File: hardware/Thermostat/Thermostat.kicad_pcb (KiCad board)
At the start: 2 copper layers, 111.2 x 76.5 mm, 46 parts, among them J1 Barrel_Jack_Switch, J2 Conn_01x02_Pin, J3 AVR-ISP-6, J4 MainConnectorr, K1 G6E, K2 G6E, K3 G6E, K4 G6E, SW1 12MM, SW2 12MM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

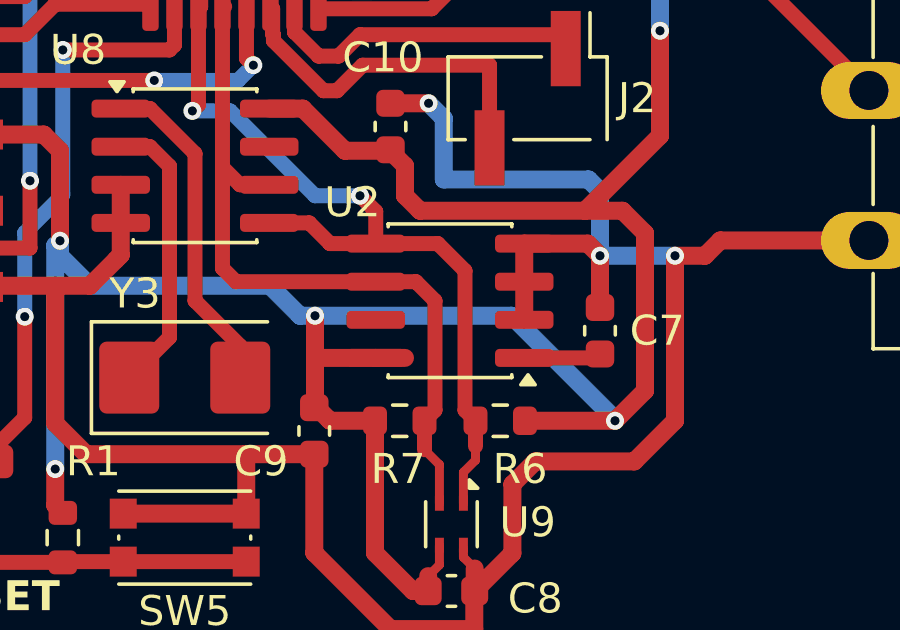
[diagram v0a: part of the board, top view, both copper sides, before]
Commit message: Integrate 47L04
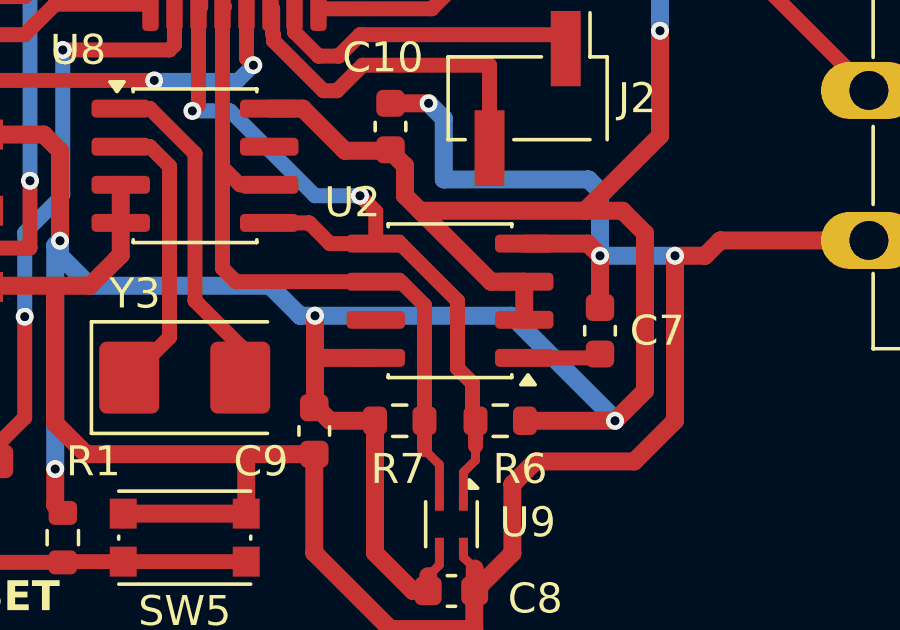
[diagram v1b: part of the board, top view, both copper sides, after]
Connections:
- U2 pad 2: GND -> +5V
- U2 pad 3: GND -> +5V
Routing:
- net +5V: track 189.7 -> 194.4 mm
- net GND: track 476.3 -> 473.8 mm
- net I2C_SDA: track 78.3 -> 77.6 mm
- net I2C_SCL: track 76.8 -> 76.3 mm
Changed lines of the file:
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@@
 			(layers "F.Cu" "F.Mask" "F.Paste")
 			(roundrect_rratio 0.25)
-			(net 1 "GND")
+			(net 3 "+5V")
 			(pinfunction "A1")
 			(pintype "input")
@@
 			(layers "F.Cu" "F.Mask" "F.Paste")
 			(roundrect_rratio 0.25)
-			(net 1 "GND")
+			(net 3 "+5V")
 			(pinfunction "A2")
 			(pintype "input")
@@
 	)
 	(segment
-		(start 195.975 110.595)
-		(end 195.975 113.135)
-		(width 0.6)
-		(layer "F.Cu")
-		(net 1)
-	)
-	(segment
 		(start 140.958 121.188)
 		(end 141.05 121.096)
@@
 	)
 	(segment
+		(start 195.975 111.865)
+		(end 195.975 113.135)
+		(width 0.6)
+		(layer "F.Cu")
+		(net 3)
+	)
+	(segment
 		(start 188.595 106.095)
 		(end 190 107.5)
@@
 	)
 	(segment
-		(start 191.999999 114.405)
-		(end 191.025 114.405)
+		(start 194.865 111.865)
+		(end 195.975 111.865)
+		(width 0.6)
+		(layer "F.Cu")
+		(net 3)
+	)
+	(segment
+		(start 192.5 109.5)
+		(end 194.865 111.865)
 		(width 0.6)
 		(layer "F.Cu")
@@
 	)
 	(segment
-		(start 194 111.5)
-		(end 194 116.15)
-		(width 0.5)
-		(layer "F.Cu")
-		(net 20)
-	)
-	(segment
 		(start 193.948 118.218)
 		(end 194.35 117.816)
@@
 	)
 	(segment
-		(start 194.35 117.348)
-		(end 194.35 116.5)
+		(start 193.75 112.5)
+		(end 193.75 114.75)
 		(width 0.5)
 		(layer "F.Cu")
@@
 	)
 	(segment
-		(start 188.214 58.418)
-		(end 185.003 55.207)
+		(start 194.35 117.348)
+		(end 194.35 116.5)
 		(width 0.5)
 		(layer "F.Cu")
@@
 	)
 	(segment
-		(start 191.025 110.595)
-		(end 193.095 110.595)
+		(start 188.214 58.418)
+		(end 185.003 55.207)
 		(width 0.5)
 		(layer "F.Cu")
@@
 	)
 	(segment
-		(start 193.095 110.595)
-		(end 194 111.5)
+		(start 191.845 110.595)
+		(end 193.75 112.5)
 		(width 0.5)
 		(layer "F.Cu")
@@
 	)
 	(segment
+		(start 194.25 115.25)
+		(end 194.25 116.4)
+		(width 0.5)
+		(layer "F.Cu")
+		(net 20)
+	)
+	(segment
 		(start 185.166 79.248)
 		(end 185.166 88.392)
@@
 	)
 	(segment
-		(start 189.5 110.595)
-		(end 191.025 110.595)
+		(start 193.75 114.75)
+		(end 194.25 115.25)
+		(width 0.5)
+		(layer "F.Cu")
+		(net 20)
+	)
+	(segment
+		(start 194.25 116.4)
+		(end 194.35 116.5)
+		(width 0.5)
+		(layer "F.Cu")
+		(net 20)
+	)
+	(segment
+		(start 191.025 110.595)
+		(end 191.845 110.595)
 		(width 0.5)
 		(layer "F.Cu")
@@
 	(segment
 		(start 189.5 110.595)
-		(end 188.81 109.905)
+		(end 191.025 110.595)
 		(width 0.5)
 		(layer "F.Cu")
@@
 	)
 	(segment
-		(start 194 116.15)
-		(end 194.35 116.5)
+		(start 189.5 110.595)
+		(end 188.81 109.905)
 		(width 0.5)
 		(layer "F.Cu")
@@
 	)
 	(segment
+		(start 191.025 111.865)
+		(end 191.865 111.865)
+		(width 0.5)
+		(layer "F.Cu")
+		(net 21)
+	)
+	(segment
 		(start 186.69 92.456)
 		(end 186.69 81.28)
@@
 	)
 	(segment
-		(start 192.65 117.466)
-		(end 193.148 117.964)
-		(width 0.3)
+		(start 191.865 111.865)
+		(end 192.65 112.65)
+		(width 0.5)
 		(layer "F.Cu")
 		(net 21)
 	)
 	(segment
-		(start 193 112.5)
-		(end 193 116.15)
-		(width 0.5)
+		(start 192.65 117.466)
+		(end 193.148 117.964)
+		(width 0.3)
 		(layer "F.Cu")
 		(net 21)
 	)
 	(segment
-		(start 192.365 111.865)
-		(end 193 112.5)
+		(start 192.65 112.65)
+		(end 192.65 116.5)
 		(width 0.5)
 		(layer "F.Cu")
@@
 		(width 0.5)
 		(layer "F.Cu")
-		(net 21)
-	)
-	(segment
-		(start 191.025 111.865)
-		(end 192.365 111.865)
-		(width 0.5)
-		(layer "F.Cu")
-		(net 21)
-	)
-	(segment
-		(start 193 116.15)
-		(end 192.65 116.5)
-		(width 0.5)
-		(layer "F.Cu")

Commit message: Battery?
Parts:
- added BT1: Battery_Cell, Battery:BatteryHolder_LINX_BAT-HLD-012-SMT, B.Cu at (172.0, 62.2)
- moved R1 0.34 mm to (180.2, 120.4)
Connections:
- U8 pad 3: GND -> Net-(BT1-+)
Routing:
- net GND: track 473.8 -> 472.5 mm

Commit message: Get in battery
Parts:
- BT1: footprint Battery:BatteryHolder_LINX_BAT-HLD-012-SMT -> Battery:BatteryHolder_Keystone_3000_1x12mm
- moved BT1 2.68 mm to (171.1, 64.8)
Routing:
- net Net-(BT1-+): track 0.00 -> 77.5 mm, vias 0 -> 1
- net GND: track 472.5 -> 481.1 mm, vias 11 -> 12
- net Net-(J3-SCK): track 25.4 -> 23.0 mm
- net +5V: track 194.0 -> 192.5 mm

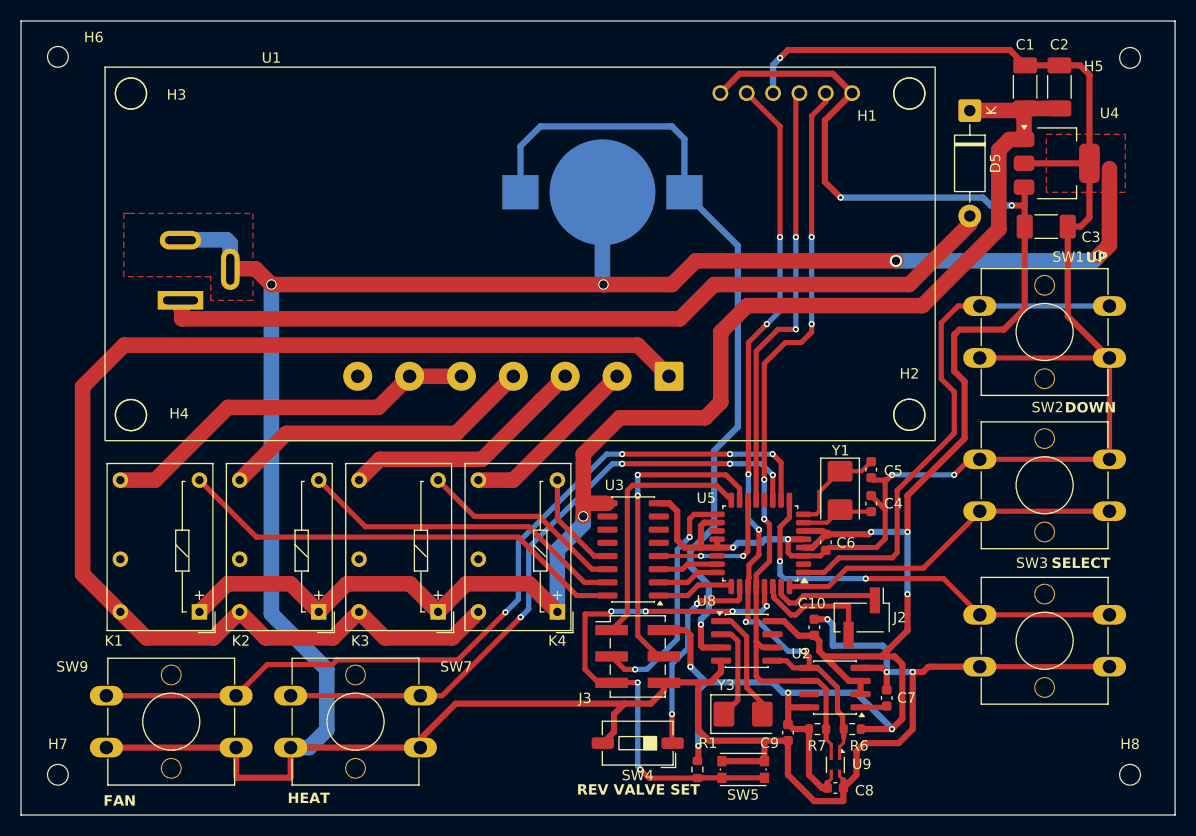
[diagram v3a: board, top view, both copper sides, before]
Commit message: Good battery and connector layout
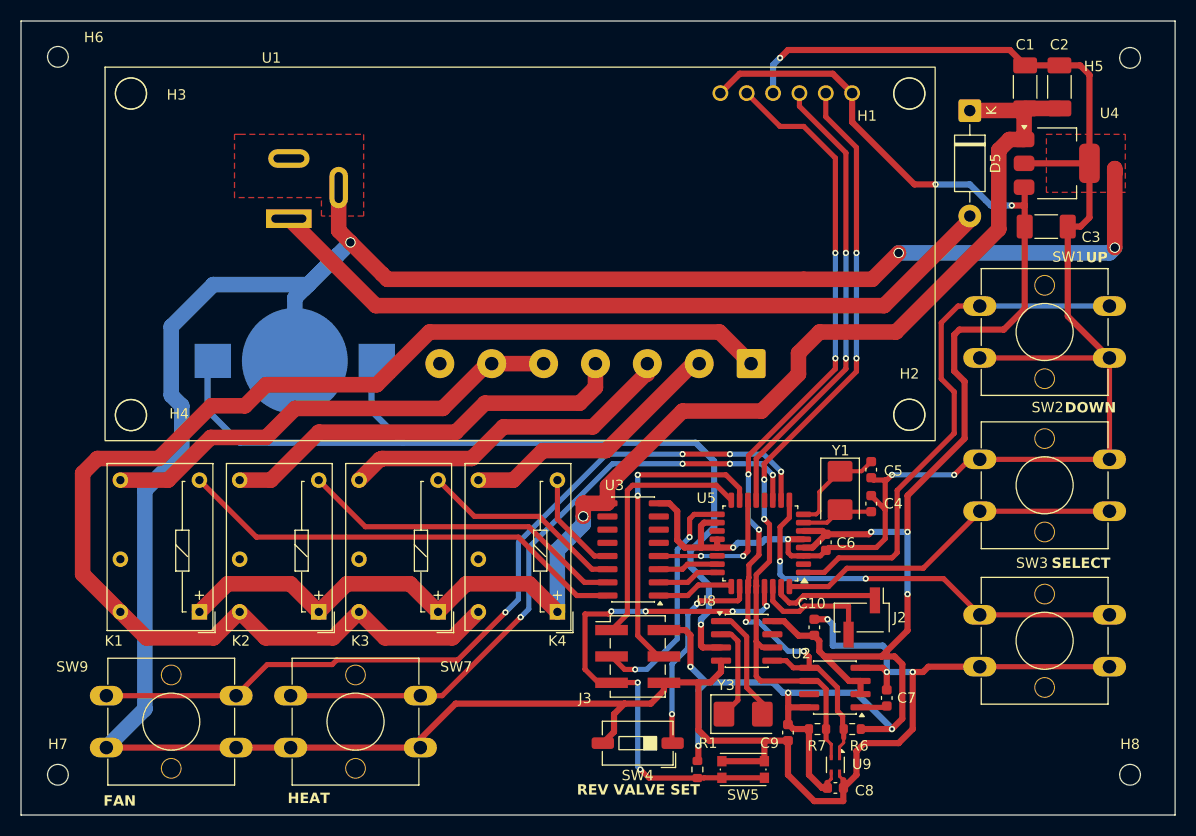
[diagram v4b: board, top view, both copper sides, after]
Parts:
- moved BT1 33.8 mm to (141.5, 81.0)
- moved J1 13.1 mm to (140.9, 67.3)
- moved J4 8.01 mm to (185.4, 81.3)
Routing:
- net Net-(J4-Pin_4): track 30.5 -> 40.3 mm
- net Net-(BT1-+): track 77.5 -> 86.6 mm
- net Net-(D5-A): track 81.6 -> 72.9 mm
- net Net-(J4-Pin_5): track 37.0 -> 45.4 mm
- net Net-(J4-Pin_2): track 17.5 -> 25.9 mm
- net Net-(J4-Pin_3): track 24.0 -> 32.0 mm
- net +5V: track 192.5 -> 185.4 mm
- net 24VDC: track 133.9 -> 127.2 mm
- net I2C_SDA: track 77.6 -> 83.3 mm
- net 24VAC: track 123.3 -> 126.9 mm
- net SCBUSY: track 42.0 -> 45.2 mm
- net GND: track 481.1 -> 482.9 mm, vias 12 -> 11
- net I2C_SCL: track 76.3 -> 77.8 mm
- net Net-(U5-PD6): track 81.9 -> 81.3 mm

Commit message: Always changes
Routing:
- net Net-(J4-Pin_4): track 40.3 -> 39.1 mm

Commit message: Fixes from Cyber City Circuits review
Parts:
- removed D5: 1N4007, Diode_THT:D_DO-41_SOD81_P10.16mm_Horizontal
- added D1: SS33, Diode_SMD:D_SMA, F.Cu at (206.0, 63.5)
- added R2: 4.7k, Resistor_SMD:R_0603_1608Metric, F.Cu at (197.4, 66.8)
- R1: value 5k -> 10k
- R6, R7: value 5k -> 4.7k
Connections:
- U1 pad 6: +5V -> ^SCRESET
- U5 pad 12: unconnected-(U5-PB0-Pad12) -> ^SCRESET
- U5 pad 18: GND -> +5V
- U5 pad 20: GND -> +5V
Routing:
- net ^SCRESET: track 0.00 -> 44.8 mm, vias 0 -> 2
- net +5V: track 185.4 -> 206.4 mm, vias 9 -> 11
- net 24VDC: track 127.2 -> 132.4 mm
- net GND: track 482.9 -> 477.7 mm
- net Net-(D1-A): track 72.9 -> 74.2 mm
- net Net-(U5-PD5): track 40.9 -> 42.0 mm
- net I2C_SCL: track 77.8 -> 78.4 mm

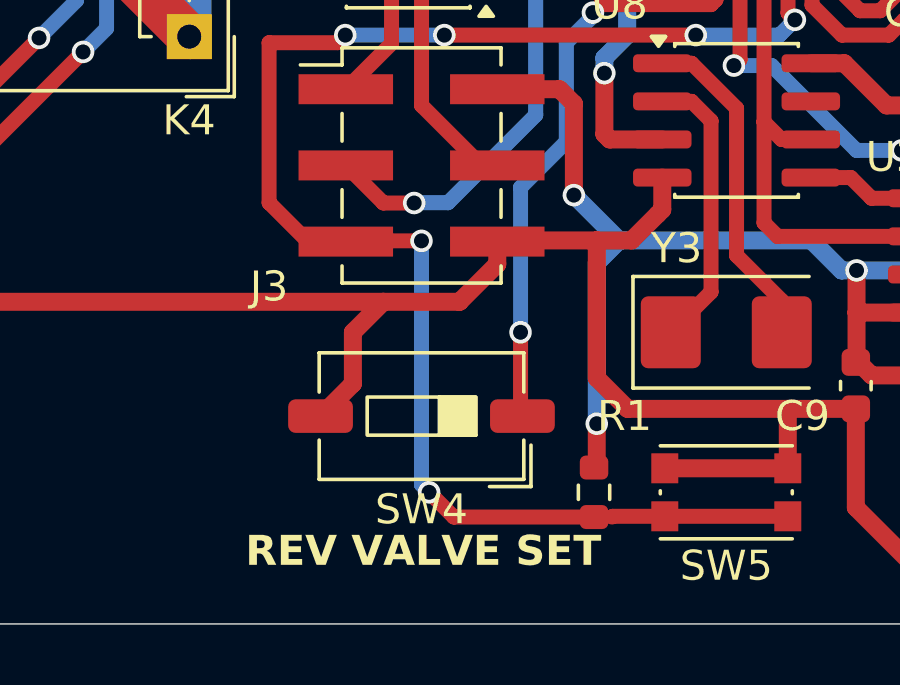
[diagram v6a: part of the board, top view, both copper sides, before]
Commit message: Remove physical Reverse Valve button and put it in save state instead
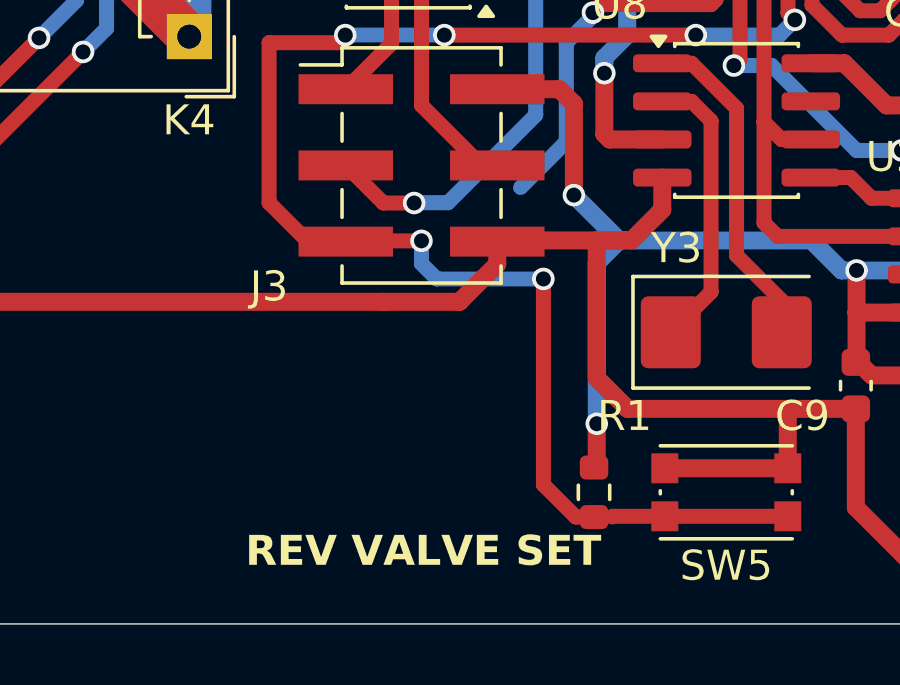
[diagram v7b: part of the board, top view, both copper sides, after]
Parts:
- removed SW4: DIP-1, Button_Switch_SMD:SW_DIP_SPSTx01_Slide_6.7x4.1mm_W6.73mm_P2.54mm_LowProfile_JPin
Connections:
- U5 pad 26: Net-(U5-PC3) -> unconnected-(U5-PC3-Pad26)
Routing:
- net Net-(U5-PC3): track 20.0 -> 0.00 mm, vias 2 -> 0
- net unconnected-(U5-PC3-Pad26): track 0.00 -> 12.3 mm, vias 0 -> 1
- net GND: track 477.7 -> 473.0 mm
- net ^RESET: track 51.3 -> 50.7 mm
